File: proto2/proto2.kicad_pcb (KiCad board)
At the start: 2 copper layers, 205.2 x 110 mm, 219 parts, among them J1 Output 1, J10 Output, J11 Device, J12 Daughter Card, J2 Main Power, J3 Output, J4 Output, J5 Device, J6 Output, J7 Device, J8 Output, J9 Device, Q1 2N7002, Q10 2N7002, Q11 2N7002, Q12 2N7002, Q2 2N7002, Q3 2N7002, Q4 2N7002, Q5 2N7002, Q6 2N7002, Q7 2N7002, Q8 2N7002, Q9 2N7002, SW1 SW_DIP_x04, U1 AQY282SX, U10 AQY282SX, U11 AQY282SX, U12 AQY282SX, U13 LDO, U2 AQY282SX, U3 AQY282SX, U4 AQY282SX, U5 AQY282SX, U6 AQY282SX, U7 AQY282SX, U8 AQY282SX, U9 AQY282SX

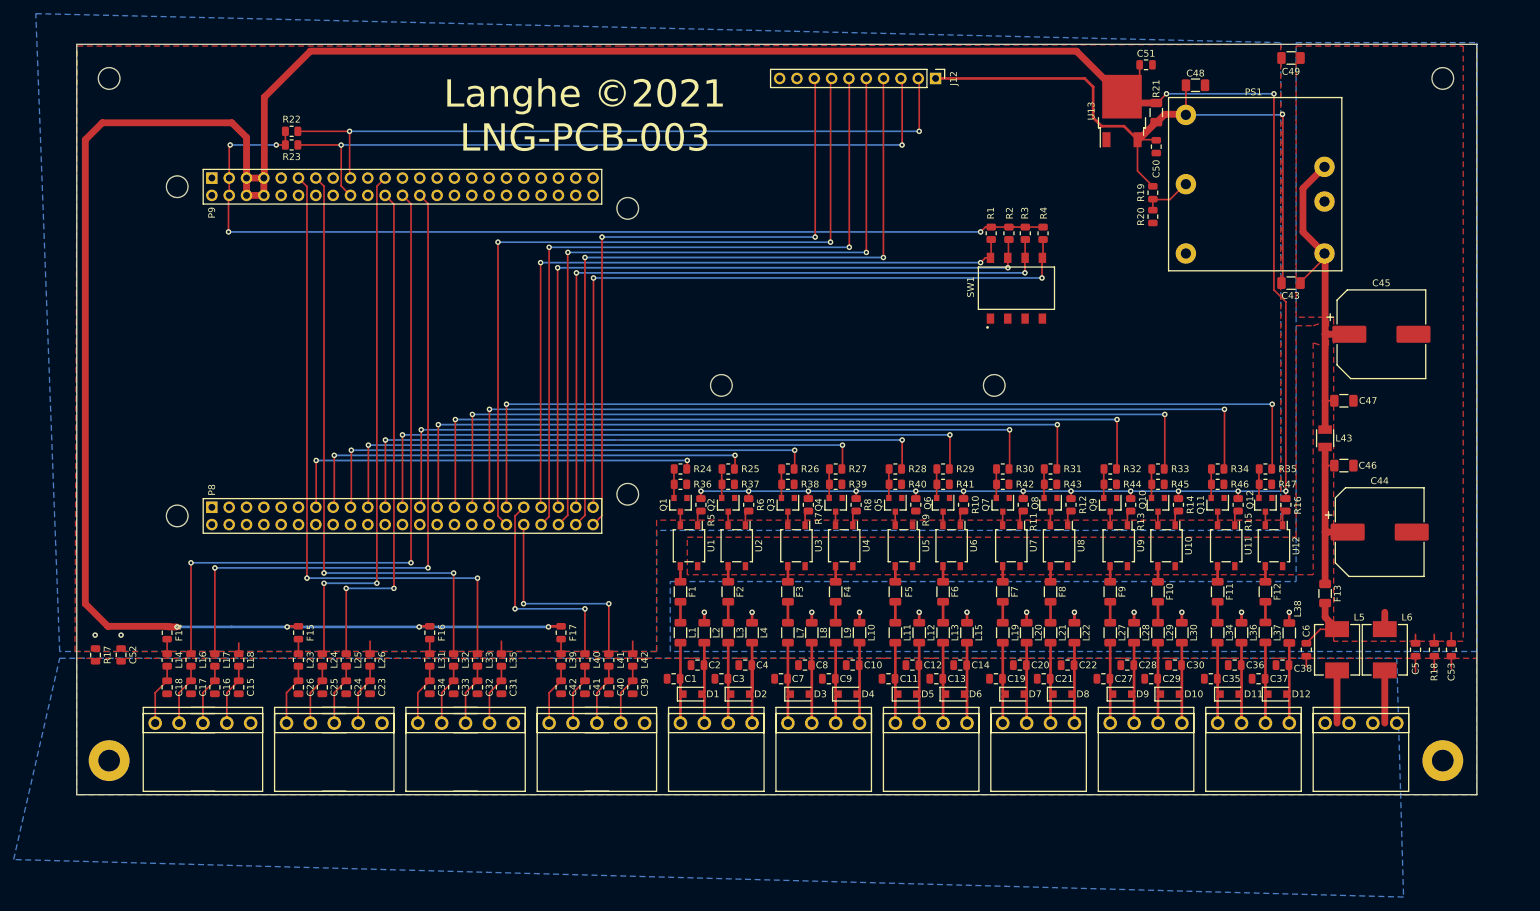
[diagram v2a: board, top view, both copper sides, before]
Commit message: Replaced LDO with a D2PAK type. Cleaned some traces.
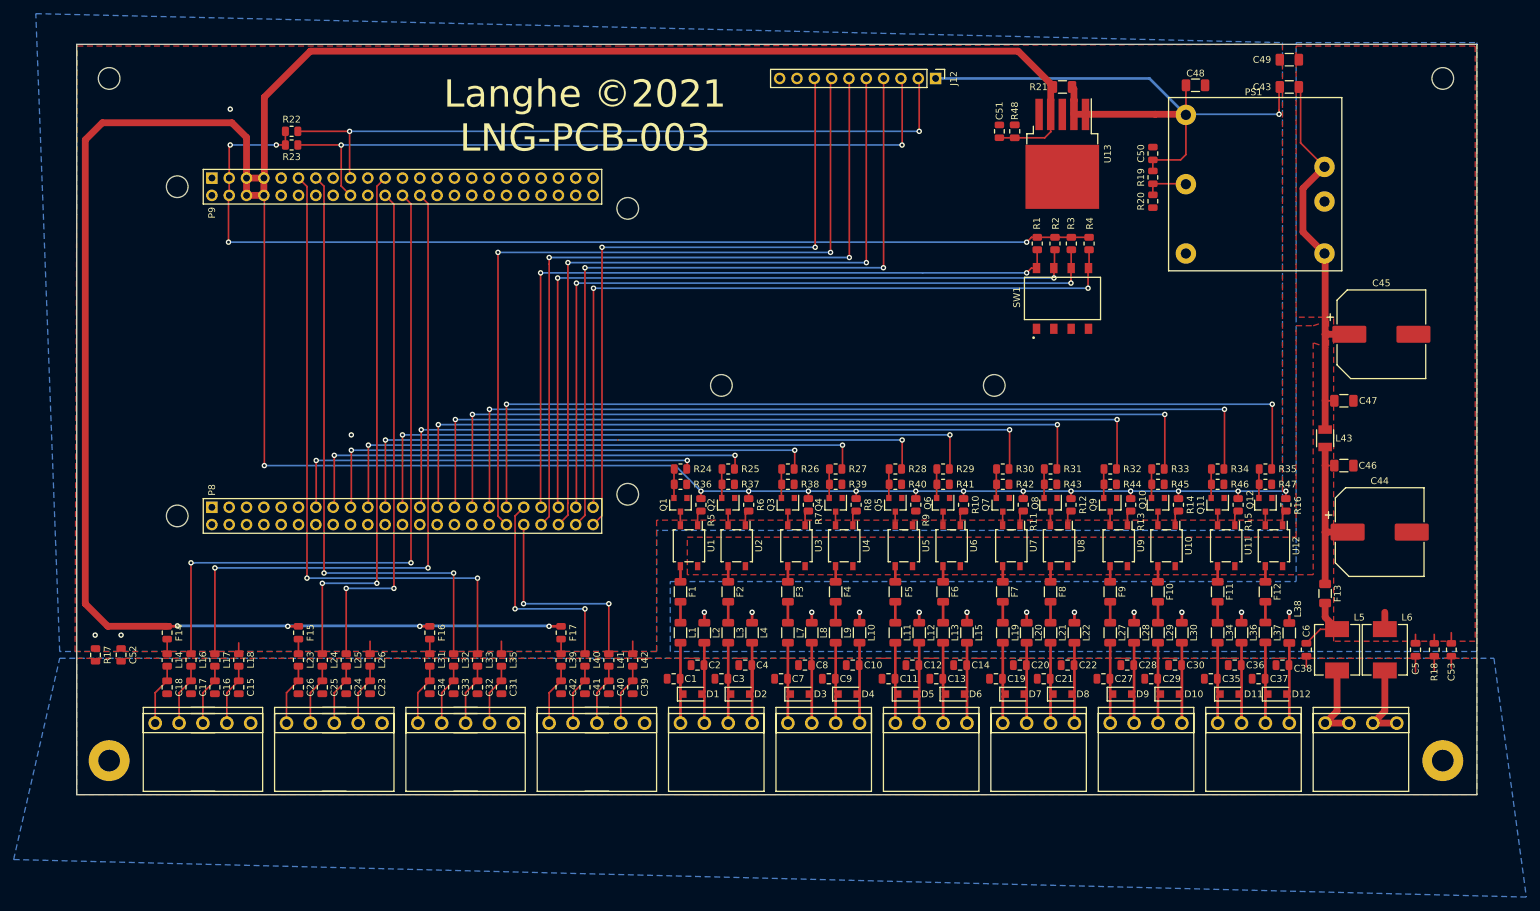
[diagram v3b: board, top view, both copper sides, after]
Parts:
- added R48: 500R, Capacitor_SMD:C_0805_2012Metric, F.Cu at (168.0, 65.8)
- C50: value 0.33uF -> 1uF
- C51: value 0.1uF -> 47uF
- U13: value LDO -> NCP59300; footprint JLCPCB:TO-252-2 -> Package_TO_SOT_SMD:TO-263-5_TabPin3
- moved C43 28.8 mm to (208.2, 59.2)
- moved C51 23.6 mm to (165.8, 65.8), turned to 90 degrees
- moved R21 14.3 mm to (175.0, 59.2), turned to 0 degrees
- moved U13 10.8 mm to (175.0, 69.0), turned to 270 degrees
- moved R1 6.91 mm to (171.3, 82.2)
- moved R2 6.91 mm to (173.9, 82.2)
- moved R3 6.91 mm to (176.3, 82.2)
- moved R4 6.91 mm to (178.9, 82.2)
- moved SW1 6.91 mm to (175.0, 90.2)
- moved R19 2.25 mm to (188.2, 72.5)
- moved R20 2.25 mm to (188.2, 76.0)
- moved C50 1.12 mm to (188.2, 69.0), turned to 90 degrees
- moved C49 0.35 mm to (208.2, 55.2)
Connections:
- U13 pad 1: GND -> VDD
- U13 pad 2: +5V -> VDD
- U13 pad 3: VDD -> GND
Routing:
- net +5V: track 509.5 -> 537.2 mm, vias 18 -> 17
- net +3V3: track 143.5 -> 151.8 mm
- net VDQ1: track 50.3 -> 58.3 mm
- net BS_4: track 105.1 -> 110.4 mm
- net BS_3: track 105.2 -> 110.4 mm
- net BS_2: track 105.5 -> 110.7 mm
- net BS_1: track 104.8 -> 110.1 mm
- net Net-(J2-Pad3): track 7.72 -> 11.9 mm
- net Net-(J2-Pad1): track 7.72 -> 11.9 mm
- net VDD: track 98.0 -> 94.4 mm
- net /Power/TRIM: track 7.24 -> 6.49 mm
- net GND: vias 2 -> 4

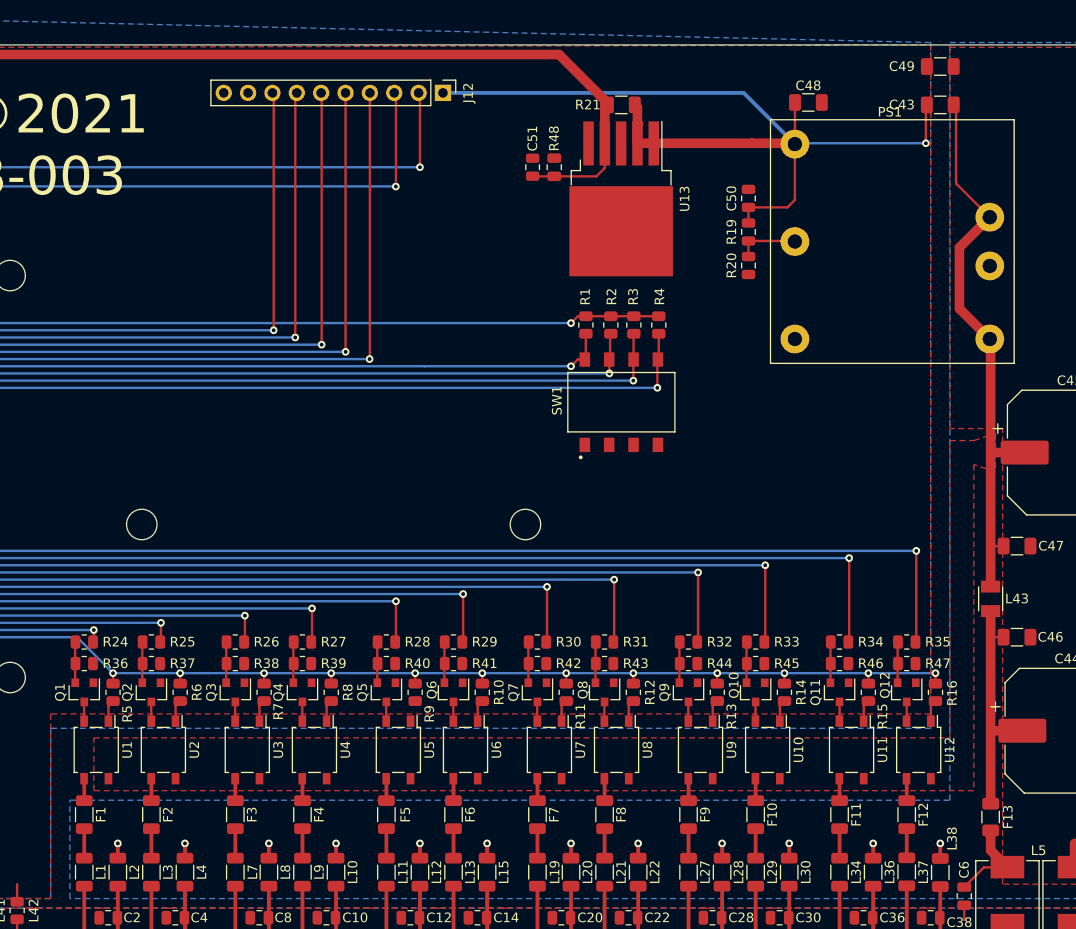
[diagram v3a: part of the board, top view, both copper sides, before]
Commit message: Added reverse polarity diode.
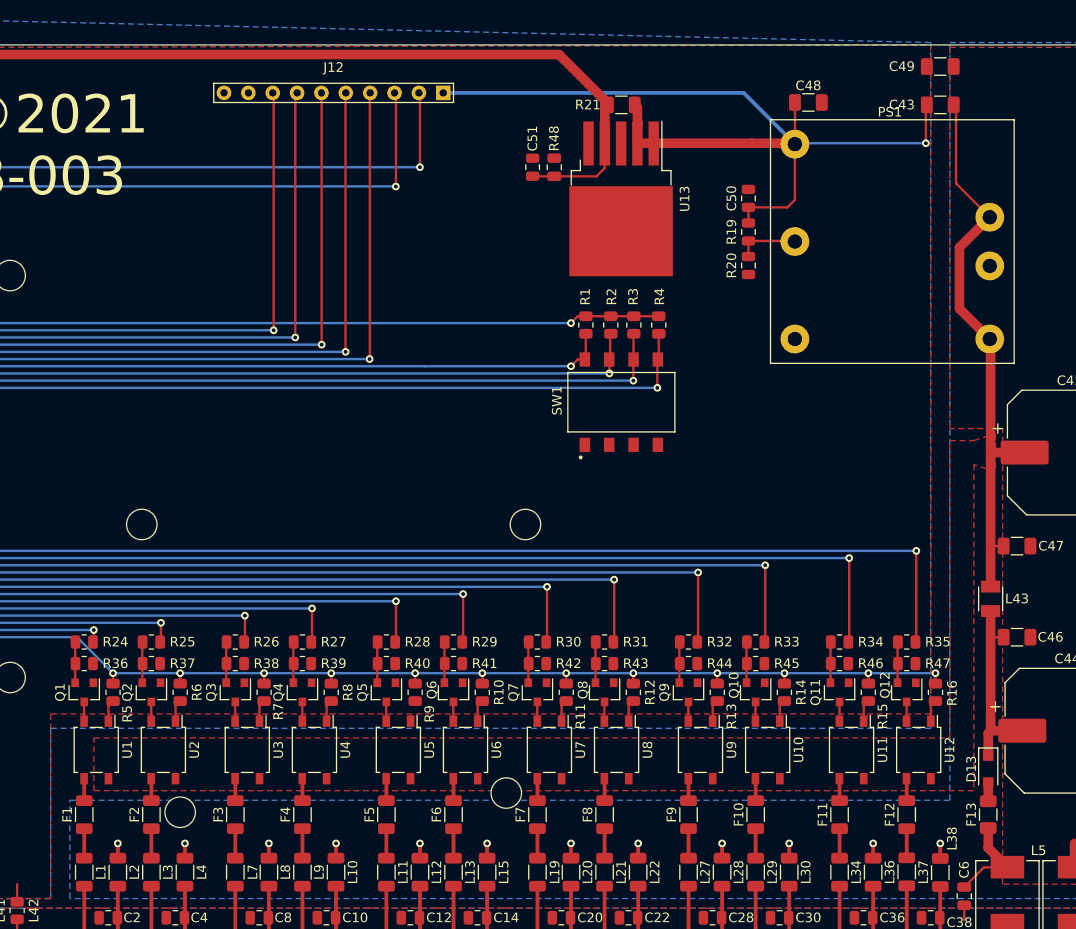
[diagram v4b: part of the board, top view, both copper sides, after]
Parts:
- removed the REF** at (165.0, 103.0)
- removed the REF** at (125.0, 103.0)
- added D13: SMA, Diode_SMD:D_SOD-123F, F.Cu at (213.2, 128.5)
- J12: footprint Connector_PinHeader_2.54mm:PinHeader_1x10_P2.54mm_Vertical -> BCR_Langhe:Proto2_DaughterCard
- moved J12 11.4 mm to (145.0, 58.0), turned to 0 degrees
- moved F13 0.35 mm to (213.2, 133.2)
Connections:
- F13 pad 1: Net-(C44-Pad1) -> Net-(D13-Pad2)
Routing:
- net Net-(C44-Pad1): track 23.5 -> 18.3 mm
- net Net-(D13-Pad2): track 0.00 -> 1.70 mm

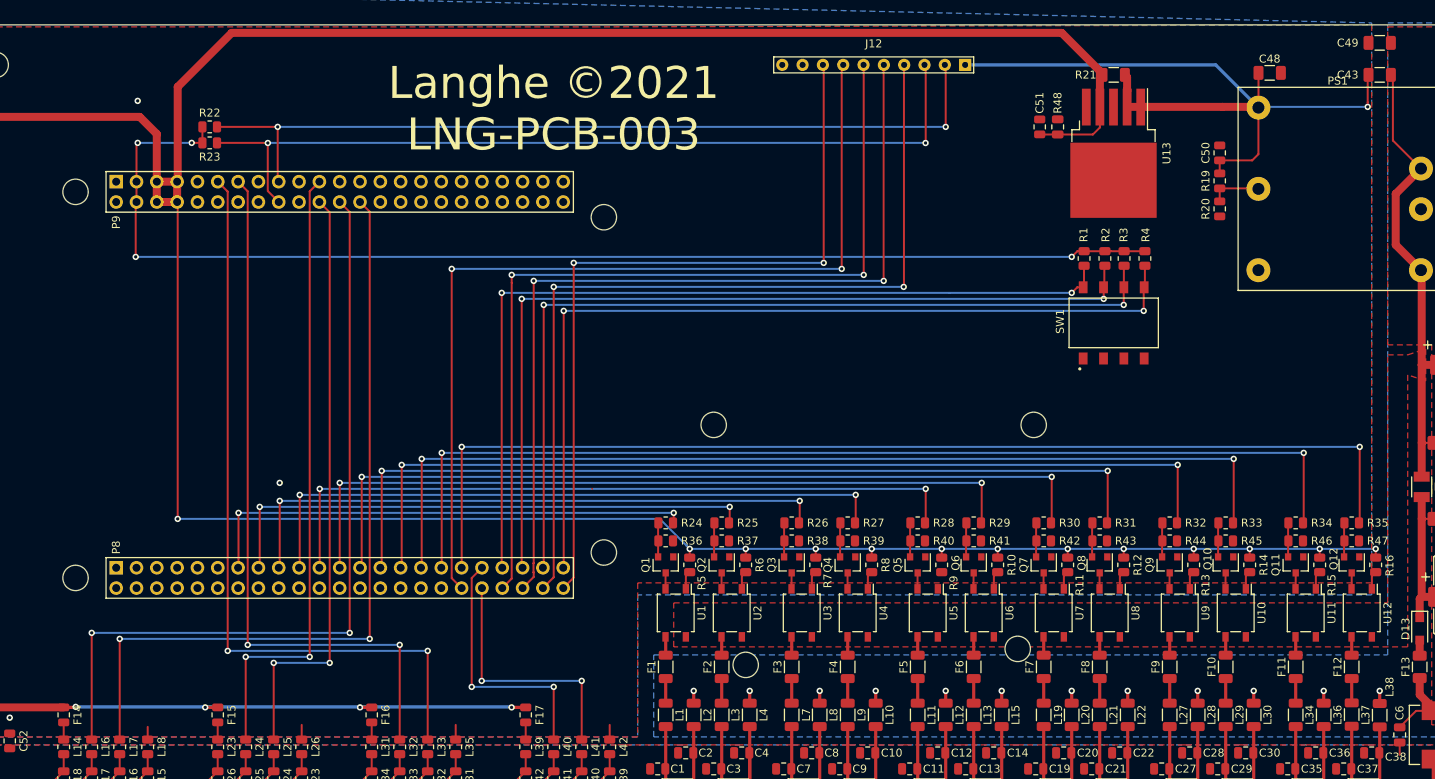
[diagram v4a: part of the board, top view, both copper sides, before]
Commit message: Updates and changes for production run of 0.1.0
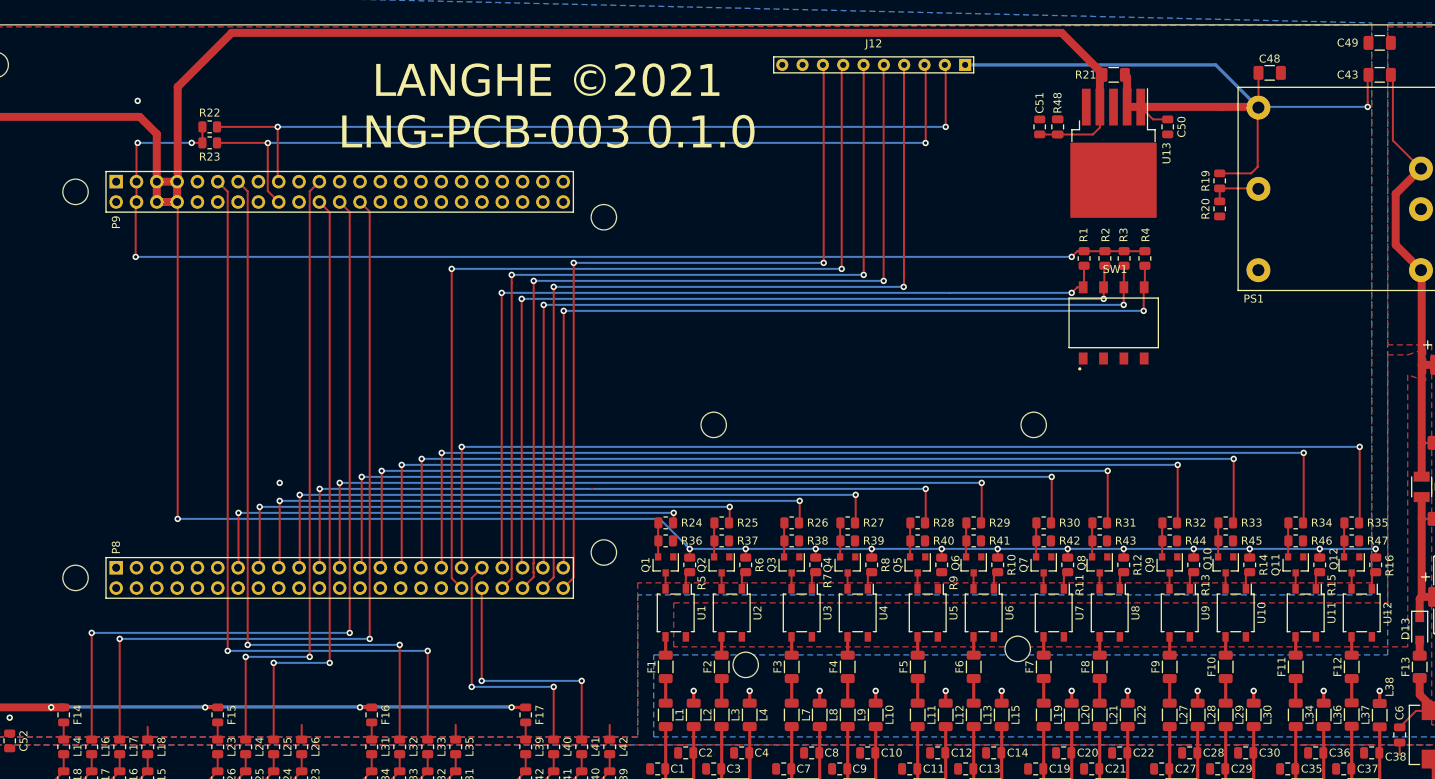
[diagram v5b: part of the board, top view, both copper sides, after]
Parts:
- SW1: footprint Button_Switch_BCR:CUI_DS04-254-2-04BK-SMT -> BCR_Switch:CUI_DS04-254-2-04BK-SMT
- moved C50 7.27 mm to (181.8, 65.8), turned to 270 degrees
- turned SW1 to 0 degrees
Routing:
- net VDD: track 94.4 -> 98.3 mm
- net +5V: track 537.2 -> 538.7 mm
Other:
- board text added: "LANGHE ©2021 LNG-PCB-003 0.1.0"
- board text removed: "Langhe ©2021 LNG-PCB-003"
